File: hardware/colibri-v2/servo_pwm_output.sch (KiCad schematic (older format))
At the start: 28 parts

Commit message: Annotated Components
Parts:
- gave numbers to parts that had none: 20

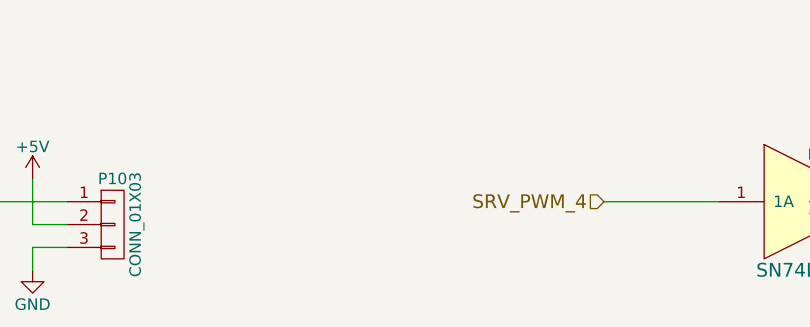
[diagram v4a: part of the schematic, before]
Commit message: Reworked the buttons/leds sheet
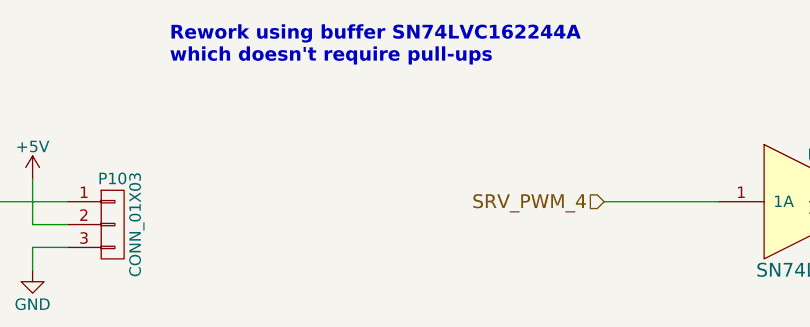
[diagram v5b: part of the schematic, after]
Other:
- note added: "Rework using buffer SN74LVC162244A\nwhich doesn't require pull-ups"
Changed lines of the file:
@@
 	0    1    1    0
 $EndComp
+Text Notes 5200 900  0    60   ~ 12
+Rework using buffer SN74LVC162244A\nwhich doesn't require pull-ups
 $EndSCHEMATC

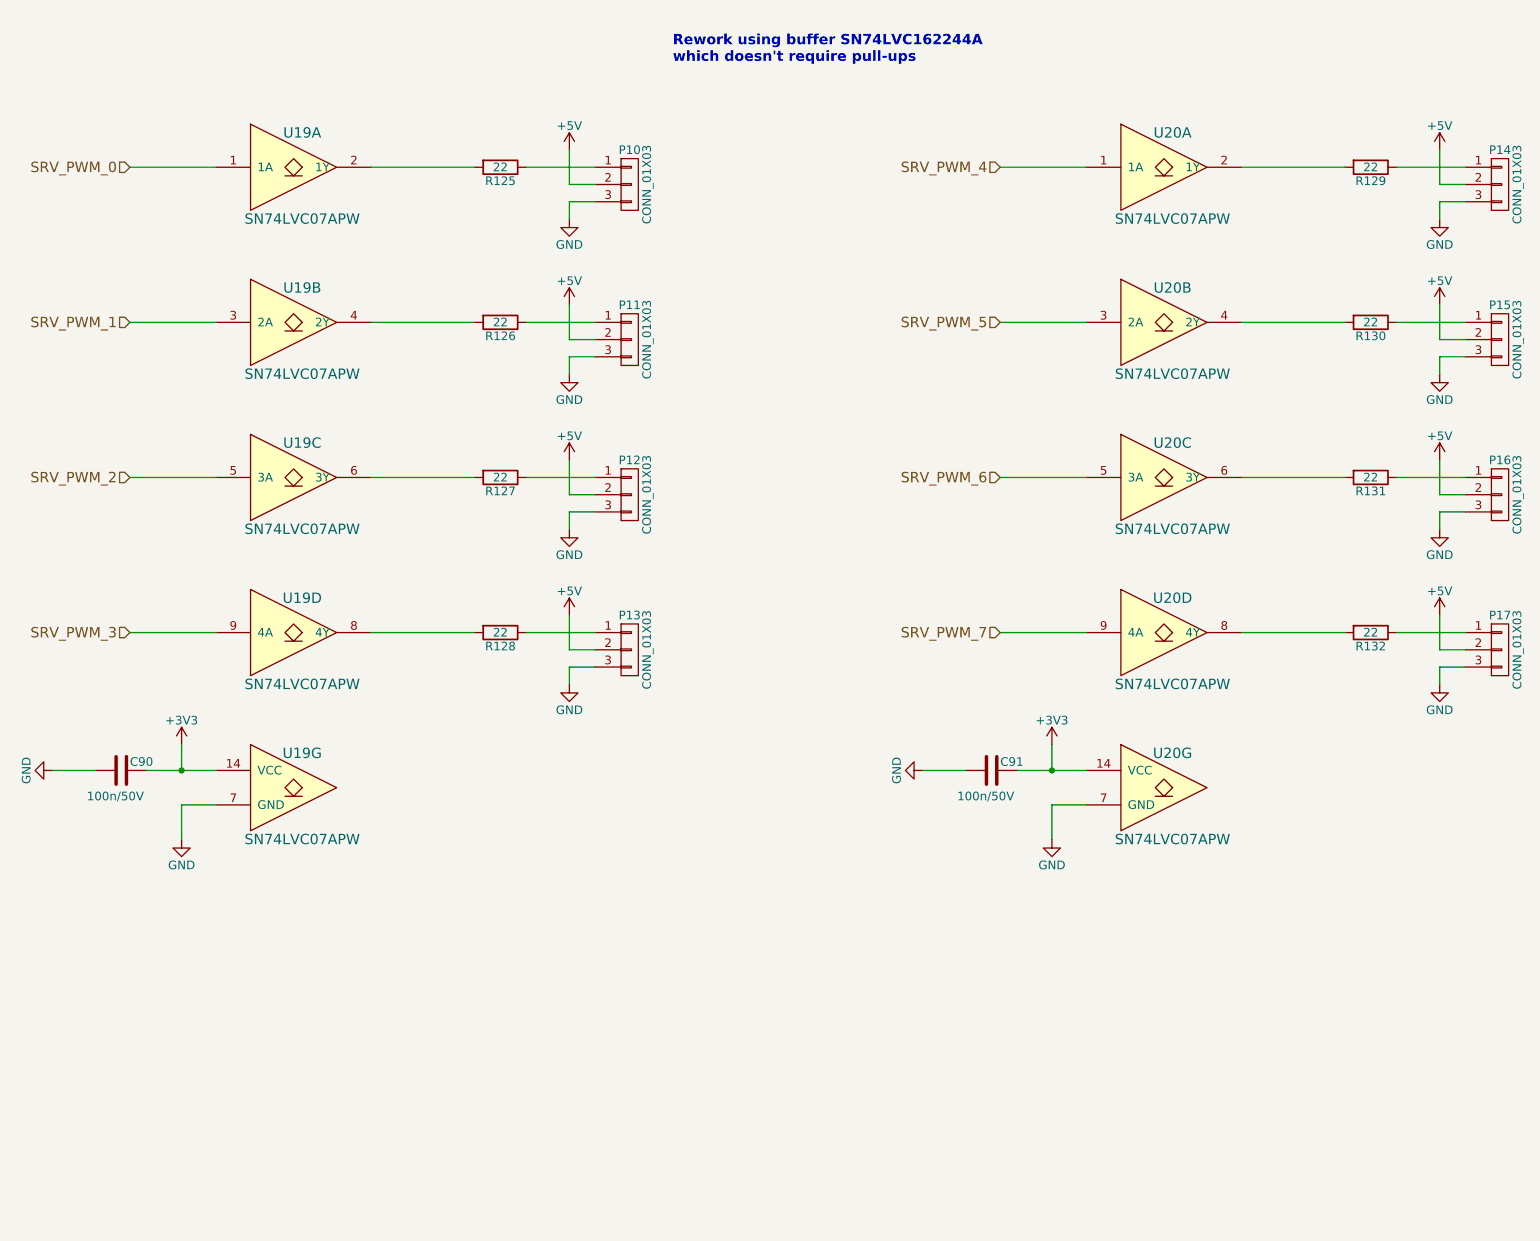
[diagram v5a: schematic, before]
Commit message: Replaced PWM buffers with SN74LVC162244A, which doesn't require pull-ups
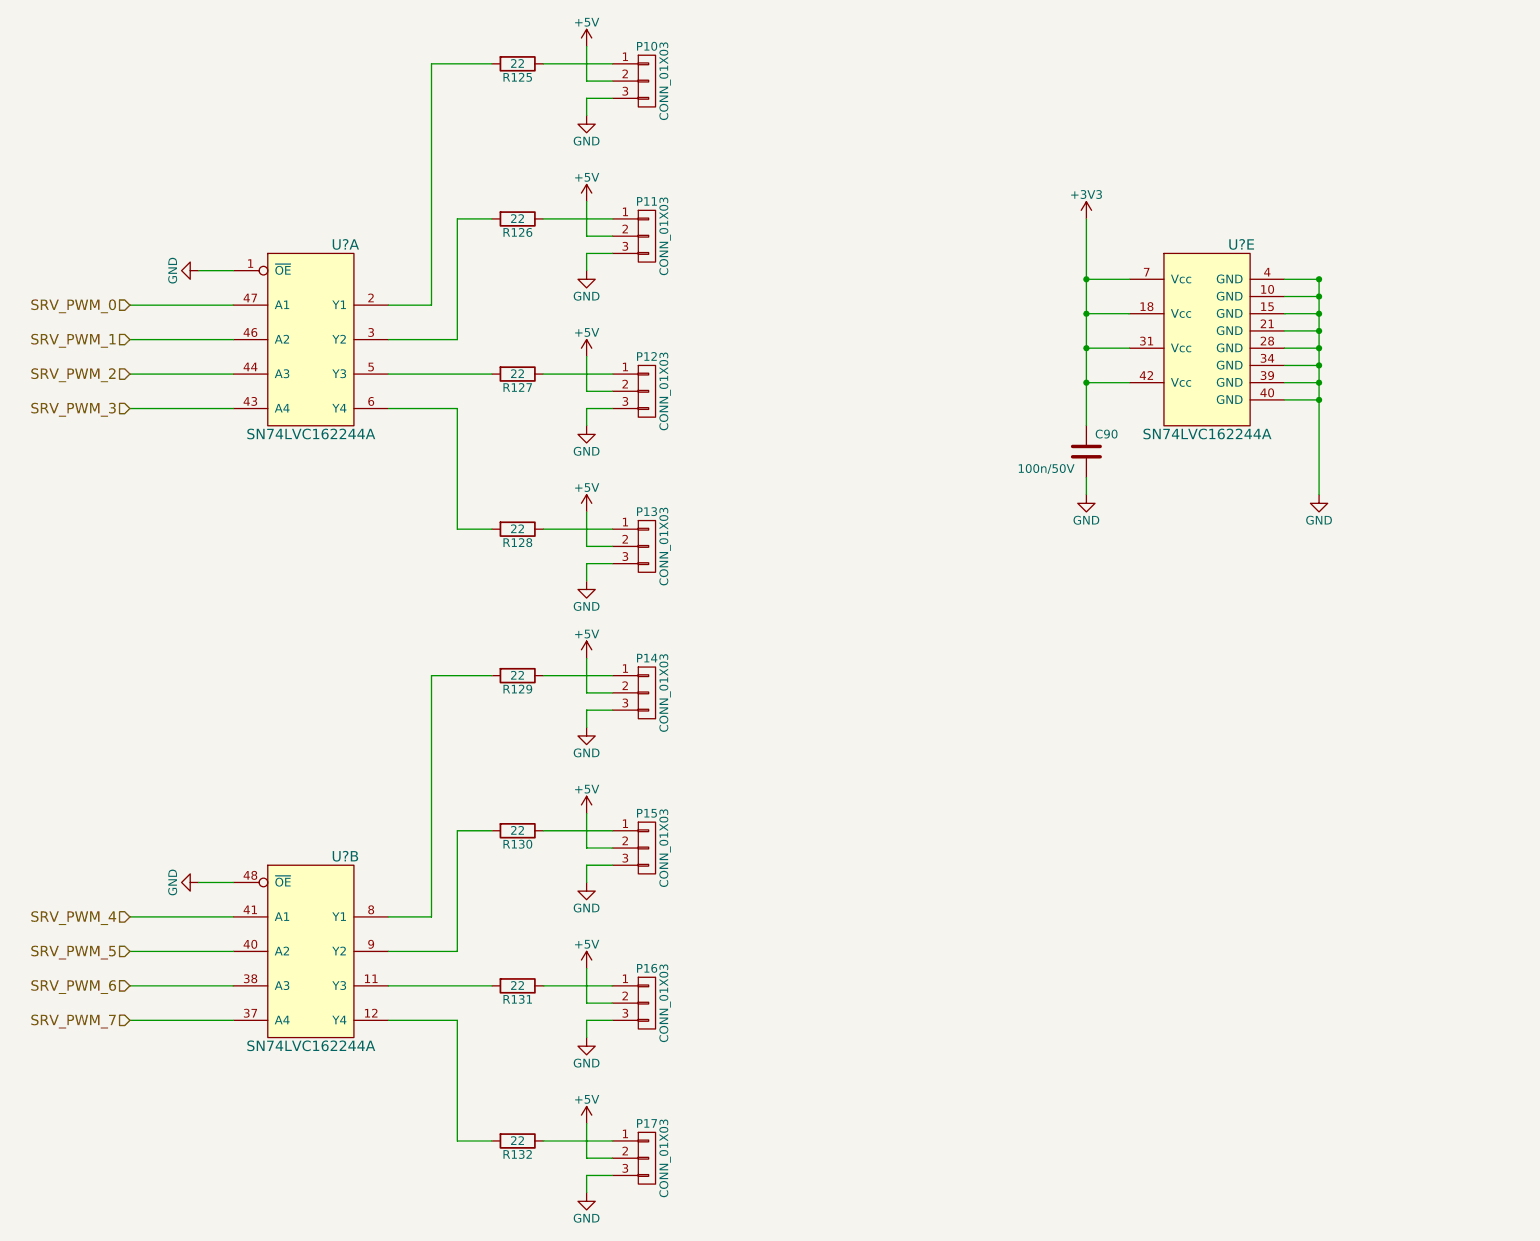
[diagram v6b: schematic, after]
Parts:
- removed C91: 100n/50V, symbol C
- removed U19, U20: SN74LVC07APW, symbol SN74LVC07APW
- added U? (x3): SN74LVC162244A, symbol SN74LVC162244A
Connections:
- net +3V3: now also U?.18 (Vcc), U?.31 (Vcc), U?.42 (Vcc), U?.7 (Vcc)
- net GND: now also U?.1 (~OE), U?.10 (GND), U?.15 (GND), U?.21 (GND), U?.28 (GND), U?.34 (GND), U?.39 (GND), U?.4 (GND), U?.40 (GND), U?.48 (~OE)
- net SRV_PWM_0: now also U?.47 (A1)
- net SRV_PWM_1: now also U?.46 (A2)
- net SRV_PWM_2: now also U?.44 (A3)
- net SRV_PWM_3: now also U?.43 (A4)
- net SRV_PWM_4: now also U?.41 (A1)
- net SRV_PWM_5: now also U?.40 (A2)
- net SRV_PWM_6: now also U?.38 (A3)
- net SRV_PWM_7: now also U?.37 (A4)
- net at R129.2: now also U?.8 (Y1)
- net at R130.2: now also U?.9 (Y2)
- net at R131.2: now also U?.11 (Y3)
- net at R132.2: now also U?.12 (Y4)
- net at R125.2: now also U?.2 (Y1)
- net at R126.2: now also U?.3 (Y2)
- net at R127.2: now also U?.5 (Y3)
- net at R128.2: now also U?.6 (Y4)
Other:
- note removed: "Rework using buffer SN74LVC162244A\nwhich doesn't require pull-ups"
- moved on the sheet: C90, P10, P11, P12, P13, P14, P15, P16, P17, R125, R126, R127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

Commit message: Re-annotated schematic
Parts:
- gave numbers to parts that had none: 1
- renumbered C90 to C88, R125 to R128, R126 to R129, R127 to R130, R128 to R131, R129 to R132, R130 to R133, R131 to R134, R132 to R135
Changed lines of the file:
@@
 $EndComp
 $Comp
-L +5V #PWR0163
+L +5V #PWR169
 U 1 1 561914C0
 P 4700 4350
-F 0 "#PWR0163" H 4700 4200 50  0001 C CNN
+F 0 "#PWR169" H 4700 4200 50  0001 C CNN
 F 1 "+5V" H 4700 4490 50  0000 C CNN
 F 2 "" H 4700 4350 60  0000 C CNN
@@
 $EndComp
 $Comp
-L GND #PWR0164
+L GND #PWR170
 U 1 1 56191507
 P 4700 4750
-F 0 "#PWR0164" H 4700 4500 50  0001 C CNN
+F 0 "#PWR170" H 4700 4500 50  0001 C CNN
 F 1 "GND" H 4700 4600 50  0000 C CNN
 F 2 "" H 4700 4750 60  0000 C CNN
@@
 $EndComp
 $Comp
-L R R129
+L R R132
 U 1 1 5619166B
 P 4300 4450
-F 0 "R129" V 4380 4450 50  0000 C CNN
+F 0 "R132" V 4380 4450 50  0000 C CNN
 F 1 "22" V 4300 4450 50  0000 C CNN
 F 2 "" V 4230 4450 30  0000 C CNN
@@
 $EndComp
 $Comp
-L +5V #PWR0165
+L +5V #PWR171
 U 1 1 56191928
 P 4700 5250
-F 0 "#PWR0165" H 4700 5100 50  0001 C CNN
+F 0 "#PWR171" H 4700 5100 50  0001 C CNN
 F 1 "+5V" H 4700 5390 50  0000 C CNN
 F 2 "" H 4700 5250 60  0000 C CNN
@@
 $EndComp
 $Comp
-L GND #PWR0166
+L GND #PWR172
 U 1 1 5619192E
 P 4700 5650
-F 0 "#PWR0166" H 4700 5400 50  0001 C CNN
+F 0 "#PWR172" H 4700 5400 50  0001 C CNN
 F 1 "GND" H 4700 5500 50  0000 C CNN
 F 2 "" H 4700 5650 60  0000 C CNN
@@
 $EndComp
 $Comp
-L R R130
+L R R133
 U 1 1 56191934
 P 4300 5350
-F 0 "R130" V 4380 5350 50  0000 C CNN
+F 0 "R133" V 4380 5350 50  0000 C CNN
 F 1 "22" V 4300 5350 50  0000 C CNN
 F 2 "" V 4230 5350 30  0000 C CNN
@@
 $EndComp
 $Comp
-L +5V #PWR0167
+L +5V #PWR173
 U 1 1 56191B28
 P 4700 6150
-F 0 "#PWR0167" H 4700 6000 50  0001 C CNN
+F 0 "#PWR173" H 4700 6000 50  0001 C CNN
 F 1 "+5V" H 4700 6290 50  0000 C CNN
 F 2 "" H 4700 6150 60  0000 C CNN
@@
 $EndComp
 $Comp
-L GND #PWR0168
+L GND #PWR174
 U 1 1 56191B2E
 P 4700 6550
-F 0 "#PWR0168" H 4700 6300 50  0001 C CNN
+F 0 "#PWR174" H 4700 6300 50  0001 C CNN
 F 1 "GND" H 4700 6400 50  0000 C CNN
 F 2 "" H 4700 6550 60  0000 C CNN
@@
 $EndComp
 $Comp
-L R R131
+L R R134
 U 1 1 56191B34
 P 4300 6250
-F 0 "R131" V 4380 6250 50  0000 C CNN
+F 0 "R134" V 4380 6250 50  0000 C CNN
 F 1 "22" V 4300 6250 50  0000 C CNN
 F 2 "" V 4230 6250 30  0000 C CNN
@@
 $EndComp
 $Comp
-L +5V #PWR0169
+L +5V #PWR175
 U 1 1 56191CEC
 P 4700 7050
-F 0 "#PWR0169" H 4700 6900 50  0001 C CNN
+F 0 "#PWR175" H 4700 6900 50  0001 C CNN
 F 1 "+5V" H 4700 7190 50  0000 C CNN
 F 2 "" H 4700 7050 60  0000 C CNN
@@
 $EndComp
 $Comp
-L GND #PWR0170
+L GND #PWR176
 U 1 1 56191CF2
 P 4700 7450
-F 0 "#PWR0170" H 4700 7200 50  0001 C CNN
+F 0 "#PWR176" H 4700 7200 50  0001 C CNN
 F 1 "GND" H 4700 7300 50  0000 C CNN
 F 2 "" H 4700 7450 60  0000 C CNN
@@
 $EndComp
 $Comp
-L R R132
+L R R135
 U 1 1 56191CF8
 P 4300 7150
-F 0 "R132" V 4380 7150 50  0000 C CNN
+F 0 "R135" V 4380 7150 50  0000 C CNN
 F 1 "22" V 4300 7150 50  0000 C CNN
 F 2 "" V 4230 7150 30  0000 C CNN
@@
 $EndComp
 $Comp
-L +5V #PWR0174
+L +5V #PWR161
 U 1 1 56193403
 P 4700 800
-F 0 "#PWR0174" H 4700 650 50  0001 C CNN
+F 0 "#PWR161" H 4700 650 50  0001 C CNN
 F 1 "+5V" H 4700 940 50  0000 C CNN
 F 2 "" H 4700 800 60  0000 C CNN
@@
 $EndComp
 $Comp
-L GND #PWR0175
+L GND #PWR162
 U 1 1 56193409
 P 4700 1200
-F 0 "#PWR0175" H 4700 950 50  0001 C CNN
+F 0 "#PWR162" H 4700 950 50  0001 C CNN
 F 1 "GND" H 4700 1050 50  0000 C CNN
 F 2 "" H 4700 1200 60  0000 C CNN
@@
 $EndComp
 $Comp
-L R R125
+L R R128
 U 1 1 5619340F
 P 4300 900
-F 0 "R125" V 4380 900 50  0000 C CNN
+F 0 "R128" V 4380 900 50  0000 C CNN
 F 1 "22" V 4300 900 50  0000 C CNN
 F 2 "" V 4230 900 30  0000 C CNN
@@
 $EndComp
 $Comp
-L +5V #PWR0176
+L +5V #PWR163
 U 1 1 56193429
 P 4700 1700
-F 0 "#PWR0176" H 4700 1550 50  0001 C CNN
+F 0 "#PWR163" H 4700 1550 50  0001 C CNN
 F 1 "+5V" H 4700 1840 50  0000 C CNN
 F 2 "" H 4700 1700 60  0000 C CNN
@@
 $EndComp
 $Comp
-L GND #PWR0177
+L GND #PWR164
 U 1 1 5619342F
 P 4700 2100
-F 0 "#PWR0177" H 4700 1850 50  0001 C CNN
+F 0 "#PWR164" H 4700 1850 50  0001 C CNN
 F 1 "GND" H 4700 1950 50  0000 C CNN
 F 2 "" H 4700 2100 60  0000 C CNN
@@
 $EndComp
 $Comp
-L R R126
+L R R129
 U 1 1 56193435
 P 4300 1800
-F 0 "R126" V 4380 1800 50  0000 C CNN
+F 0 "R129" V 4380 1800 50  0000 C CNN
 F 1 "22" V 4300 1800 50  0000 C CNN
 F 2 "" V 4230 1800 30  0000 C CNN
@@
 $EndComp
 $Comp
-L +5V #PWR0178
+L +5V #PWR165
 U 1 1 5619344F
 P 4700 2600
-F 0 "#PWR0178" H 4700 2450 50  0001 C CNN
+F 0 "#PWR165" H 4700 2450 50  0001 C CNN
 F 1 "+5V" H 4700 2740 50  0000 C CNN
 F 2 "" H 4700 2600 60  0000 C CNN
@@
 $EndComp
 $Comp
-L GND #PWR0179
+L GND #PWR166
 U 1 1 56193455
 P 4700 3000
-F 0 "#PWR0179" H 4700 2750 50  0001 C CNN
+F 0 "#PWR166" H 4700 2750 50  0001 C CNN
 F 1 "GND" H 4700 2850 50  0000 C CNN
 F 2 "" H 4700 3000 60  0000 C CNN
@@
 $EndComp
 $Comp
-L R R127
+L R R130
 U 1 1 5619345B
 P 4300 2700
-F 0 "R127" V 4380 2700 50  0000 C CNN
+F 0 "R130" V 4380 2700 50  0000 C CNN
 F 1 "22" V 4300 2700 50  0000 C CNN
 F 2 "" V 4230 2700 30  0000 C CNN
@@
 $EndComp
 $Comp
-L +5V #PWR0180
+L +5V #PWR167
 U 1 1 56193475
 P 4700 3500
-F 0 "#PWR0180" H 4700 3350 50  0001 C CNN
+F 0 "#PWR167" H 4700 3350 50  0001 C CNN
 F 1 "+5V" H 4700 3640 50  0000 C CNN
 F 2 "" H 4700 3500 60  0000 C CNN
@@
 $EndComp
 $Comp
-L GND #PWR0181
+L GND #PWR168
 U 1 1 5619347B
 P 4700 3900
-F 0 "#PWR0181" H 4700 3650 50  0001 C CNN
+F 0 "#PWR168" H 4700 3650 50  0001 C CNN
 F 1 "GND" H 4700 3750 50  0000 C CNN
 F 2 "" H 4700 3900 60  0000 C CNN
@@
 $EndComp
 $Comp
-L R R128
+L R R131
 U 1 1 56193481
 P 4300 3600
-F 0 "R128" V 4380 3600 50  0000 C CNN
+F 0 "R131" V 4380 3600 50  0000 C CNN
 F 1 "22" V 4300 3600 50  0000 C CNN
 F 2 "" V 4230 3600 30  0000 C CNN
@@
 SRV_PWM_3
 $Comp
-L +3V3 #PWR0183
+L +3V3 #PWR177
 U 1 1 5619349D
 P 7600 1800
-F 0 "#PWR0183" H 7600 1650 50  0001 C CNN
+F 0 "#PWR177" H 7600 1650 50  0001 C CNN
 F 1 "+3V3" H 7600 1940 50  0000 C CNN
 F 2 "" H 7600 1800 60  0000 C CNN
@@
 $EndComp
 $Comp
-L GND #PWR0184
+L GND #PWR178
 U 1 1 561934AB
 P 7600 3400
-F 0 "#PWR0184" H 7600 3150 50  0001 C CNN
+F 0 "#PWR178" H 7600 3150 50  0001 C CNN
 F 1 "GND" H 7600 3250 50  0000 C CNN
 F 2 "" H 7600 3400 60  0000 C CNN
@@
 $EndComp
 $Comp
-L C C90
+L C C88
 U 1 1 5619436E
 P 7600 3150
-F 0 "C90" H 7650 3250 50  0000 L CNN
+F 0 "C88" H 7650 3250 50  0000 L CNN
 F 1 "100n/50V" H 7200 3050 50  0000 L CNN
 F 2 "" H 7638 3000 30  0000 C CNN
@@
 $EndComp
 $Comp
-L SN74LVC162244A U?
+L SN74LVC162244A U19
 U 1 1 56245EEA
 P 3100 2500
-F 0 "U?" H 3300 3050 60  0000 C CNN
+F 0 "U19" H 3300 3050 60  0000 C CNN
 F 1 "SN74LVC162244A" H 3100 1950 60  0000 C CNN
 F 2 "" H 3100 2350 60  0000 C CNN
@@
 $EndComp
 $Comp
-L GND #PWR?
+L GND #PWR159
 U 1 1 56246310
 P 2450 2100
-F 0 "#PWR?" H 2450 1850 50  0001 C CNN
+F 0 "#PWR159" H 2450 1850 50  0001 C CNN
 F 1 "GND" H 2450 1950 50  0000 C CNN
 F 2 "" H 2450 2100 60  0000 C CNN
@@
 $EndComp
 $Comp
-L SN74LVC162244A U?
+L SN74LVC162244A U19
 U 2 1 5624684B
 P 3100 6050
-F 0 "U?" H 3300 6600 60  0000 C CNN
+F 0 "U19" H 3300 6600 60  0000 C CNN
 F 1 "SN74LVC162244A" H 3100 5500 60  0000 C CNN
 F 2 "" H 3100 5900 60  0000 C CNN
@@
 $EndComp
 $Comp
-L SN74LVC162244A U?
-U 5 1 562469AD
+L SN74LVC162244A U19
+U 3 1 562469AD
 P 8300 2500
-F 0 "U?" H 8500 3050 60  0000 C CNN
+F 0 "U19" H 8500 3050 60  0000 C CNN
 F 1 "SN74LVC162244A" H 8300 1950 60  0000 C CNN
 F 2 "" H 8300 2350 60  0000 C CNN
 F 3 "" H 8300 2350 60  0000 C CNN
-	5    8300 2500
-	1    0    0    -1
-$EndComp
-$Comp
-L GND #PWR?
+	3    8300 2500
+	1    0    0    -1
+$EndComp
+$Comp
+L GND #PWR179
 U 1 1 56246B43
 P 8950 3400
-F 0 "#PWR?" H 8950 3150 50  0001 C CNN
+F 0 "#PWR179" H 8950 3150 50  0001 C CNN
 F 1 "GND" H 8950 3250 50  0000 C CNN
 F 2 "" H 8950 3400 60  0000 C CNN
@@
 $EndComp
 $Comp
-L GND #PWR?
+L GND #PWR160
 U 1 1 5624E422
 P 2450 5650
-F 0 "#PWR?" H 2450 5400 50  0001 C CNN
+F 0 "#PWR160" H 2450 5400 50  0001 C CNN
 F 1 "GND" H 2450 5500 50  0000 C CNN
 F 2 "" H 2450 5650 60  0000 C CNN
